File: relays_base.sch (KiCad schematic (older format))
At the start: 10 parts, among them J1 Conn_01x02, J2 Conn_01x02, J3 Conn_01x03, J4 Conn_01x04, J5 Conn_01x02, Q1 Q_NMOS_SGD

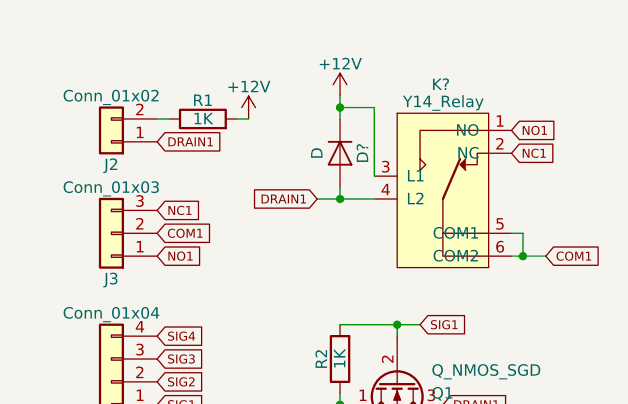
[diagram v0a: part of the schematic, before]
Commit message: Assign footprint for one relay schema with using kicad library
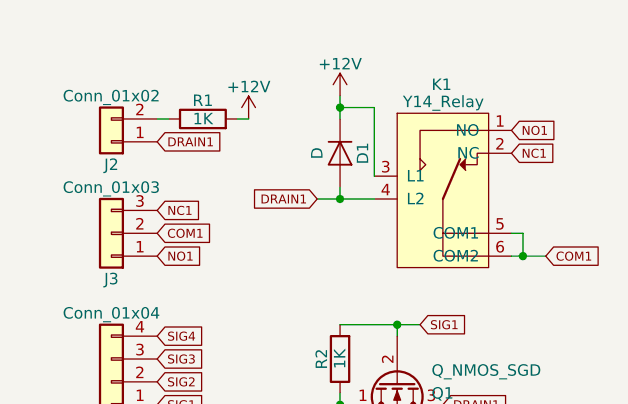
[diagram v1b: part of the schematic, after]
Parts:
- removed K?: Y14_Relay, Relays_THT:Y14H_Series_Relay, symbol Y14_Relay
- added K1: Y14_Relay, Relays_THT:Relay_Y14, symbol Y14_Relay
- D1: renamed from D?; footprint (none) -> Diodes_THT:D_A-405_P7.62mm_Horizontal
- J1, J2, J5: footprint (none) -> Socket_Strips:Socket_Strip_Straight_1x02_Pitch2.54mm
- J3: footprint (none) -> Socket_Strips:Socket_Strip_Straight_1x03_Pitch2.54mm
- J4: footprint (none) -> Socket_Strips:Socket_Strip_Straight_1x04_Pitch2.00mm
- Q1: footprint (none) -> TO_SOT_Packages_THT:TO-92_Inline_Narrow_Oval
- R1, R2: footprint (none) -> Resistors_THT:R_Axial_DIN0204_L3.6mm_D1.6mm_P5.08mm_Horizontal
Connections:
- net +12V: now also K1.3 (L1)
- net COM1: now also K1.5 (COM1), K1.6 (COM2)
- net DRAIN1: now also K1.4 (L2)
- net NC1: now also K1.2 (NC)
- net NO1: now also K1.1 (NO)
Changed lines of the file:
@@
 LIBS:Relay
 LIBS:Connector
-LIBS:y14_relay
 LIBS:relays_base-cache
 EELAYER 25 0
@@
 F 0 "Q1" V 5200 5150 50  0000 L CNN
 F 1 "Q_NMOS_SGD" V 5100 5150 50  0000 L CNN
-F 2 "" H 5350 5100 50  0001 C CNN
+F 2 "TO_SOT_Packages_THT:TO-92_Inline_Narrow_Oval" H 5350 5100 50  0001 C CNN
 F 3 "" H 5150 5000 50  0001 C CNN
 	1    5150 5000
@@
 $EndComp
 $Comp
-L GND #PWR6
+L GND #PWR7
 U 1 1 5A327DB6
 P 4900 5150
-F 0 "#PWR6" H 4900 4900 50  0001 C CNN
+F 0 "#PWR7" H 4900 4900 50  0001 C CNN
 F 1 "GND" H 4900 5000 50  0000 C CNN
 F 2 "" H 4900 5150 50  0001 C CNN
@@
 $EndComp
 $Comp
-L +12V #PWR7
+L +12V #PWR6
 U 1 1 5A327E0C
 P 4900 3750
-F 0 "#PWR7" H 4900 3600 50  0001 C CNN
+F 0 "#PWR6" H 4900 3600 50  0001 C CNN
 F 1 "+12V" H 4900 3890 50  0000 C CNN
 F 2 "" H 4900 3750 50  0001 C CNN
@@
 F 0 "R2" V 4980 4900 50  0000 C CNN
 F 1 "1K" V 4900 4900 50  0000 C CNN
-F 2 "" V 4830 4900 50  0001 C CNN
+F 2 "Resistors_THT:R_Axial_DIN0204_L3.6mm_D1.6mm_P5.08mm_Horizontal" V 4830 4900 50  0001 C CNN
 F 3 "" H 4900 4900 50  0001 C CNN
 	1    4900 4900
@@
 F 0 "J4" H 3900 5200 50  0000 C CNN
 F 1 "Conn_01x04" H 3900 4700 50  0000 C CNN
-F 2 "" H 3900 5000 50  0001 C CNN
+F 2 "Socket_Strips:Socket_Strip_Straight_1x04_Pitch2.00mm" H 3900 5000 50  0001 C CNN
 F 3 "" H 3900 5000 50  0001 C CNN
 	1    3900 5000
@@
 F 0 "R1" V 4380 3850 50  0000 C CNN
 F 1 "1K" V 4300 3850 50  0000 C CNN
-F 2 "" V 4230 3850 50  0001 C CNN
+F 2 "Resistors_THT:R_Axial_DIN0204_L3.6mm_D1.6mm_P5.08mm_Horizontal" V 4230 3850 50  0001 C CNN
 F 3 "" H 4300 3850 50  0001 C CNN
 	1    4300 3850
@@
 F 0 "J2" H 3900 4050 50  0000 C CNN
 F 1 "Conn_01x02" H 3900 3750 50  0000 C CNN
-F 2 "" H 3900 3950 50  0001 C CNN
+F 2 "Socket_Strips:Socket_Strip_Straight_1x02_Pitch2.54mm" H 3900 3950 50  0001 C CNN
 F 3 "" H 3900 3950 50  0001 C CNN
 	1    3900 3950
@@
 F 0 "J3" H 3900 4550 50  0000 C CNN
 F 1 "Conn_01x03" H 3900 4150 50  0000 C CNN
-F 2 "" H 3900 4350 50  0001 C CNN
+F 2 "Socket_Strips:Socket_Strip_Straight_1x03_Pitch2.54mm" H 3900 4350 50  0001 C CNN
 F 3 "" H 3900 4350 50  0001 C CNN
 	1    3900 4350
@@
 F 0 "J5" H 2650 3800 50  0000 C CNN
 F 1 "Conn_01x02" H 2650 3500 50  0000 C CNN
-F 2 "" H 2650 3700 50  0001 C CNN
+F 2 "Socket_Strips:Socket_Strip_Straight_1x02_Pitch2.54mm" H 2650 3700 50  0001 C CNN
 F 3 "" H 2650 3700 50  0001 C CNN
 	1    2650 3700
@@
 F 0 "J1" H 2650 4350 50  0000 C CNN
 F 1 "Conn_01x02" H 2650 4050 50  0000 C CNN
-F 2 "" H 2650 4250 50  0001 C CNN
+F 2 "Socket_Strips:Socket_Strip_Straight_1x02_Pitch2.54mm" H 2650 4250 50  0001 C CNN
 F 3 "" H 2650 4250 50  0001 C CNN
 	1    2650 4250
@@
 	1    0    0    -1
 $EndComp
-$Comp
-L Y14_Relay K?
-U 1 1 5A32C74A
-P 5350 4150
-F 0 "K?" H 5300 4600 50  0000 L CNN
-F 1 "Y14_Relay" H 5175 4525 50  0000 L CNN
-F 2 "Relays_THT:Y14H_Series_Relay" H 5375 3750 50  0001 C CNN
-F 3 "" H 4650 3500 50  0001 C CNN
-	1    5350 4150
-	1    0    0    -1
-$EndComp
 Text GLabel 5800 4450 2    39   Input ~ 0
 COM1
 $Comp
-L D D?
+L D D1
 U 1 1 5A32C90E
 P 4900 4000
-F 0 "D?" H 4900 4100 50  0000 C CNN
+F 0 "D1" H 4900 4100 50  0000 C CNN
 F 1 "D" H 4900 3900 50  0000 C CNN
-F 2 "" H 4900 4000 50  0001 C CNN
+F 2 "Diodes_THT:D_A-405_P7.62mm_Horizontal" H 4900 4000 50  0001 C CNN
 F 3 "" H 4900 4000 50  0001 C CNN
 	1    4900 4000
@@
 	5050 3800 4900 3800
 Connection ~ 4900 3800
+$Comp
+L Y14_Relay K1
+U 1 1 5A33CE6D
+P 5350 4150
+F 0 "K1" H 5300 4600 50  0000 L CNN
+F 1 "Y14_Relay" H 5175 4525 50  0000 L CNN
+F 2 "Relays_THT:Relay_Y14" H 5375 3750 50  0001 C CNN
+F 3 "" H 4650 3500 50  0001 C CNN
+	1    5350 4150
+	1    0    0    -1
+$EndComp
 $EndSCHEMATC

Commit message: Create schematic for 4 relays
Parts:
- removed J2: Conn_01x02, Socket_Strips:Socket_Strip_Straight_1x02_Pitch2.54mm, symbol Conn_01x02
- removed J3: Conn_01x03, Socket_Strips:Socket_Strip_Straight_1x03_Pitch2.54mm, symbol Conn_01x03
- removed K1: Y14_Relay, Relays_THT:Relay_Y14, symbol Y14_Relay
- added D2, D3, D4: D, Diode_THT:D_5W_P10.16mm_Horizontal, symbol D
- added J4, J5, J6, J7: Conn_01x05, Connector_PinHeader_2.54mm:PinHeader_1x05_P2.54mm_Vertical, symbol Conn_01x05
- added JP1, JP2, JP3, JP4: Jumper_NO, Jumper:SolderJumper_01x02, symbol Jumper_NO_Small
- added K1, K2, K3, K4: Y14, Relay_THT:Relay_Y14, symbol Y14
- added Q2, Q3, Q4: Q_NMOS_SGD, Package_TO_SOT_THT:TO-92_Inline, symbol Q_NMOS_SGD
- added R3, R4, R5, R6, R7, R8: 1K, Resistor_THT:R_Axial_DIN0207_L6.3mm_D2.5mm_P7.62mm_Horizontal, symbol R-RESCUE-relays_base
- D1: footprint Diodes_THT:D_A-405_P7.62mm_Horizontal -> Diode_THT:D_5W_P10.16mm_Horizontal
- J1: renamed from J5; footprint Socket_Strips:Socket_Strip_Straight_1x02_Pitch2.54mm -> Connector_PinHeader_2.54mm:PinHeader_1x02_P2.54mm_Vertical
- J2: renamed from J1; footprint Socket_Strips:Socket_Strip_Straight_1x02_Pitch2.54mm -> Connector_PinHeader_2.54mm:PinHeader_1x02_P2.54mm_Vertical
- J3: renamed from J4; footprint Socket_Strips:Socket_Strip_Straight_1x04_Pitch2.00mm -> Connector_PinHeader_2.54mm:PinHeader_1x04_P2.54mm_Vertical
- Q1: footprint TO_SOT_Packages_THT:TO-92_Inline_Narrow_Oval -> Package_TO_SOT_THT:TO-92_Inline
- R1, R2: footprint Resistors_THT:R_Axial_DIN0204_L3.6mm_D1.6mm_P5.08mm_Horizontal -> Resistor_THT:R_Axial_DIN0207_L6.3mm_D2.5mm_P7.62mm_Horizontal; symbol R -> R-RESCUE-relays_base
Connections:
- net +12V: now also D2.1 (K), D3.1 (K), D4.1 (K), JP1.2, JP2.2, JP3.2, JP4.2, K1.3 (L1), K2.3 (L1), K3.3 (L1), K4.3 (L1), R4.2, R6.2, R8.2
- net COM1: now also J4.2 (Pin_2), K1.5 (COM1), K1.6 (COM2)
- net DRAIN1: now also J4.4 (Pin_4), K1.4 (L2)
- net GND: now also Q2.1 (S), Q3.1 (S), Q4.1 (S), R3.1, R5.1, R7.1
- net NC1: now also J4.1 (Pin_1), K1.2 (NC)
- net NO1: now also J4.3 (Pin_3), K1.1 (NO)
- net SIG2: now also Q2.2 (G), R3.2
- net SIG3: now also Q3.2 (G), R5.2
- net SIG4: now also Q4.2 (G), R7.2
- net at R1.1: now also J4.5 (Pin_5), JP1.1
- new net: J5.5 (Pin_5), JP2.1, R4.1
- new net: J6.5 (Pin_5), JP3.1, R6.1
- new net: J7.5 (Pin_5), JP4.1, R8.1
- new net COM2: J5.2 (Pin_2), K2.5 (COM1), K2.6 (COM2)
- new net COM3: J6.2 (Pin_2), K3.5 (COM1), K3.6 (COM2)
- new net COM4: J7.2 (Pin_2), K4.5 (COM1), K4.6 (COM2)
- new net DRAIN2: D2.2 (A), J5.4 (Pin_4), K2.4 (L2), Q2.3 (D)
- new net DRAIN3: D3.2 (A), J6.4 (Pin_4), K3.4 (L2), Q3.3 (D)
- new net DRAIN4: D4.2 (A), J7.4 (Pin_4), K4.4 (L2), Q4.3 (D)
- new net NC2: J5.1 (Pin_1), K2.2 (NC)
- new net NC3: J6.1 (Pin_1), K3.2 (NC)
- new net NC4: J7.1 (Pin_1), K4.2 (NC)
- new net NO2: J5.3 (Pin_3), K2.1 (NO)
- new net NO3: J6.3 (Pin_3), K3.1 (NO)
- new net NO4: J7.3 (Pin_3), K4.1 (NO)
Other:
- moved on the sheet: D1, J1, J2, J3, Q1, R1, R2

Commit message: Design PCB with using net from schematic
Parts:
- D1, D2, D3, D4: footprint Diode_THT:D_5W_P10.16mm_Horizontal -> Diode_THT:D_A-405_P7.62mm_Horizontal
- R1, R2, R3, R4, R5, R6, R7, R8: footprint Resistor_THT:R_Axial_DIN0207_L6.3mm_D2.5mm_P7.62mm_Horizontal -> Resistor_THT:R_Axial_DIN0207_L6.3mm_D2.5mm_P2.54mm_Vertical
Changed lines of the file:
@@
 F 0 "R2" V 2780 3800 50  0000 C CNN
 F 1 "1K" V 2700 3800 50  0000 C CNN
-F 2 "Resistor_THT:R_Axial_DIN0207_L6.3mm_D2.5mm_P7.62mm_Horizontal" V 2630 3800 50  0001 C CNN
+F 2 "Resistor_THT:R_Axial_DIN0207_L6.3mm_D2.5mm_P2.54mm_Vertical" V 2630 3800 50  0001 C CNN
 F 3 "" H 2700 3800 50  0001 C CNN
 	1    2700 3800
@@
 F 0 "R1" V 3280 1450 50  0000 C CNN
 F 1 "1K" V 3200 1450 50  0000 C CNN
-F 2 "Resistor_THT:R_Axial_DIN0207_L6.3mm_D2.5mm_P7.62mm_Horizontal" V 3130 1450 50  0001 C CNN
+F 2 "Resistor_THT:R_Axial_DIN0207_L6.3mm_D2.5mm_P2.54mm_Vertical" V 3130 1450 50  0001 C CNN
 F 3 "" H 3200 1450 50  0001 C CNN
 	1    3200 1450
@@
 F 0 "D1" H 2600 2750 50  0000 C CNN
 F 1 "D" H 2600 2550 50  0000 C CNN
-F 2 "Diode_THT:D_5W_P10.16mm_Horizontal" H 2600 2650 50  0001 C CNN
+F 2 "Diode_THT:D_A-405_P7.62mm_Horizontal" H 2600 2650 50  0001 C CNN
 F 3 "" H 2600 2650 50  0001 C CNN
 	1    2600 2650
@@
 F 0 "R3" V 4430 3800 50  0000 C CNN
 F 1 "1K" V 4350 3800 50  0000 C CNN
-F 2 "Resistor_THT:R_Axial_DIN0207_L6.3mm_D2.5mm_P7.62mm_Horizontal" V 4280 3800 50  0001 C CNN
+F 2 "Resistor_THT:R_Axial_DIN0207_L6.3mm_D2.5mm_P2.54mm_Vertical" V 4280 3800 50  0001 C CNN
 F 3 "" H 4350 3800 50  0001 C CNN
 	1    4350 3800
@@
 F 0 "R4" V 4930 1450 50  0000 C CNN
 F 1 "1K" V 4850 1450 50  0000 C CNN
-F 2 "Resistor_THT:R_Axial_DIN0207_L6.3mm_D2.5mm_P7.62mm_Horizontal" V 4780 1450 50  0001 C CNN
+F 2 "Resistor_THT:R_Axial_DIN0207_L6.3mm_D2.5mm_P2.54mm_Vertical" V 4780 1450 50  0001 C CNN
 F 3 "" H 4850 1450 50  0001 C CNN
 	1    4850 1450
@@
 F 0 "D2" H 4250 2750 50  0000 C CNN
 F 1 "D" H 4250 2550 50  0000 C CNN
-F 2 "Diode_THT:D_5W_P10.16mm_Horizontal" H 4250 2650 50  0001 C CNN
+F 2 "Diode_THT:D_A-405_P7.62mm_Horizontal" H 4250 2650 50  0001 C CNN
 F 3 "" H 4250 2650 50  0001 C CNN
 	1    4250 2650
@@
 F 0 "R5" V 6130 3800 50  0000 C CNN
 F 1 "1K" V 6050 3800 50  0000 C CNN
-F 2 "Resistor_THT:R_Axial_DIN0207_L6.3mm_D2.5mm_P7.62mm_Horizontal" V 5980 3800 50  0001 C CNN
+F 2 "Resistor_THT:R_Axial_DIN0207_L6.3mm_D2.5mm_P2.54mm_Vertical" V 5980 3800 50  0001 C CNN
 F 3 "" H 6050 3800 50  0001 C CNN
 	1    6050 3800
@@
 F 0 "R6" V 6630 1450 50  0000 C CNN
 F 1 "1K" V 6550 1450 50  0000 C CNN
-F 2 "Resistor_THT:R_Axial_DIN0207_L6.3mm_D2.5mm_P7.62mm_Horizontal" V 6480 1450 50  0001 C CNN
+F 2 "Resistor_THT:R_Axial_DIN0207_L6.3mm_D2.5mm_P2.54mm_Vertical" V 6480 1450 50  0001 C CNN
 F 3 "" H 6550 1450 50  0001 C CNN
 	1    6550 1450
@@
 F 0 "D3" H 5950 2750 50  0000 C CNN
 F 1 "D" H 5950 2550 50  0000 C CNN
-F 2 "Diode_THT:D_5W_P10.16mm_Horizontal" H 5950 2650 50  0001 C CNN
+F 2 "Diode_THT:D_A-405_P7.62mm_Horizontal" H 5950 2650 50  0001 C CNN
 F 3 "" H 5950 2650 50  0001 C CNN
 	1    5950 2650
@@
 F 0 "R7" V 7780 3800 50  0000 C CNN
 F 1 "1K" V 7700 3800 50  0000 C CNN
-F 2 "Resistor_THT:R_Axial_DIN0207_L6.3mm_D2.5mm_P7.62mm_Horizontal" V 7630 3800 50  0001 C CNN
+F 2 "Resistor_THT:R_Axial_DIN0207_L6.3mm_D2.5mm_P2.54mm_Vertical" V 7630 3800 50  0001 C CNN
 F 3 "" H 7700 3800 50  0001 C CNN
 	1    7700 3800
@@
 F 0 "R8" V 8280 1450 50  0000 C CNN
 F 1 "1K" V 8200 1450 50  0000 C CNN
-F 2 "Resistor_THT:R_Axial_DIN0207_L6.3mm_D2.5mm_P7.62mm_Horizontal" V 8130 1450 50  0001 C CNN
+F 2 "Resistor_THT:R_Axial_DIN0207_L6.3mm_D2.5mm_P2.54mm_Vertical" V 8130 1450 50  0001 C CNN
 F 3 "" H 8200 1450 50  0001 C CNN
 	1    8200 1450
@@
 F 0 "D4" H 7600 2750 50  0000 C CNN
 F 1 "D" H 7600 2550 50  0000 C CNN
-F 2 "Diode_THT:D_5W_P10.16mm_Horizontal" H 7600 2650 50  0001 C CNN
+F 2 "Diode_THT:D_A-405_P7.62mm_Horizontal" H 7600 2650 50  0001 C CNN
 F 3 "" H 7600 2650 50  0001 C CNN
 	1    7600 2650
